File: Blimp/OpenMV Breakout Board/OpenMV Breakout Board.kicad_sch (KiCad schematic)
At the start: 20 parts, among them J1 UART3, J2 Detector, J3 Servo, J4 Debug, M1 OPENMV3, U1 ATWINC1500, U2 74LVC1G17

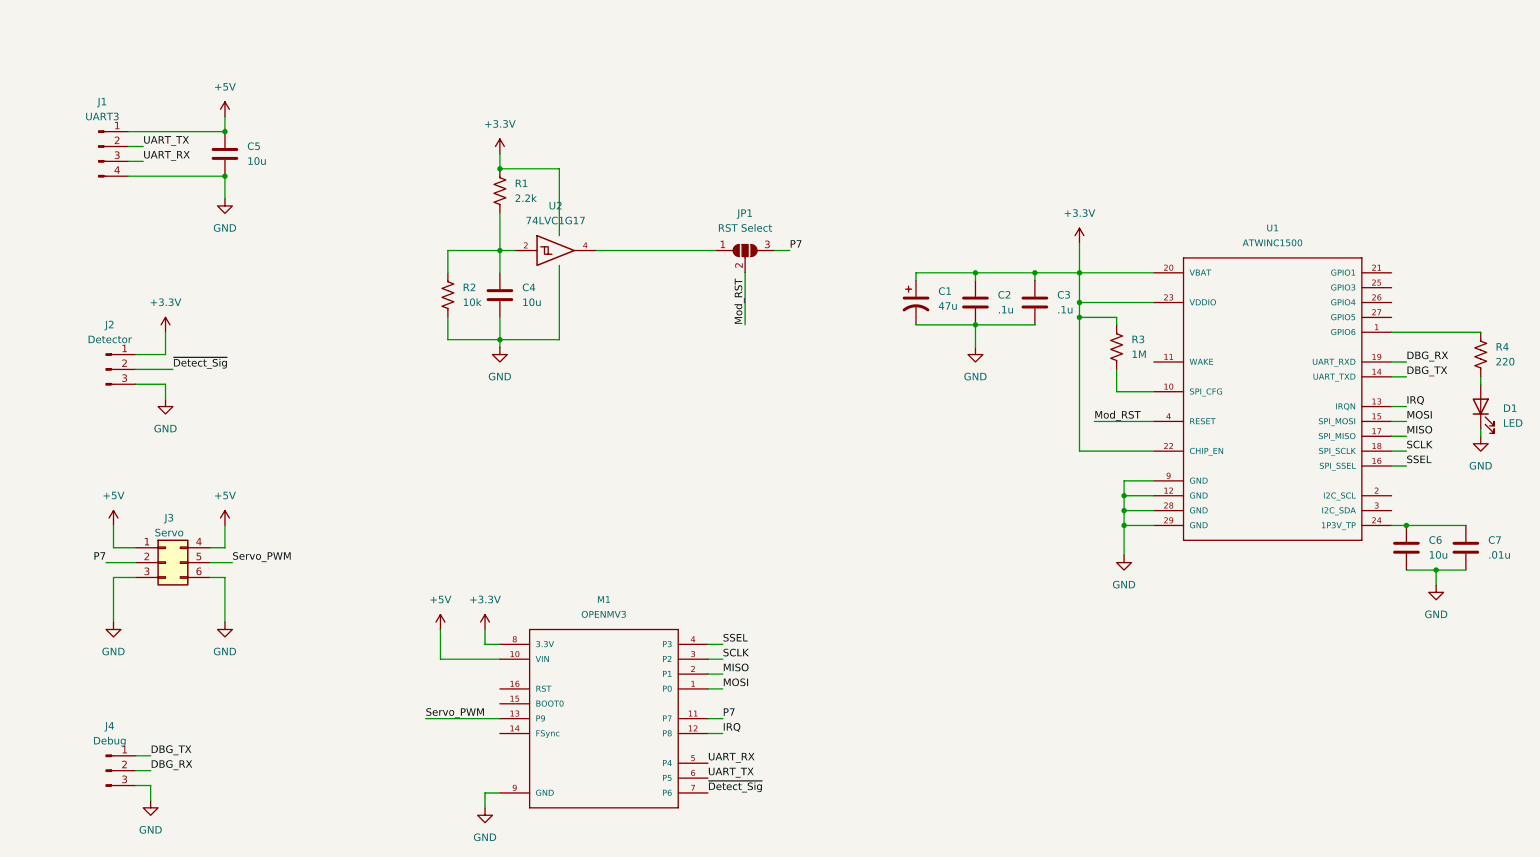
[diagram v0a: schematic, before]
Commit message: Updates to OpenMV hat to make pin labels more legible on PCB. Change schematic to be A paper sized for printing, reorg for readability
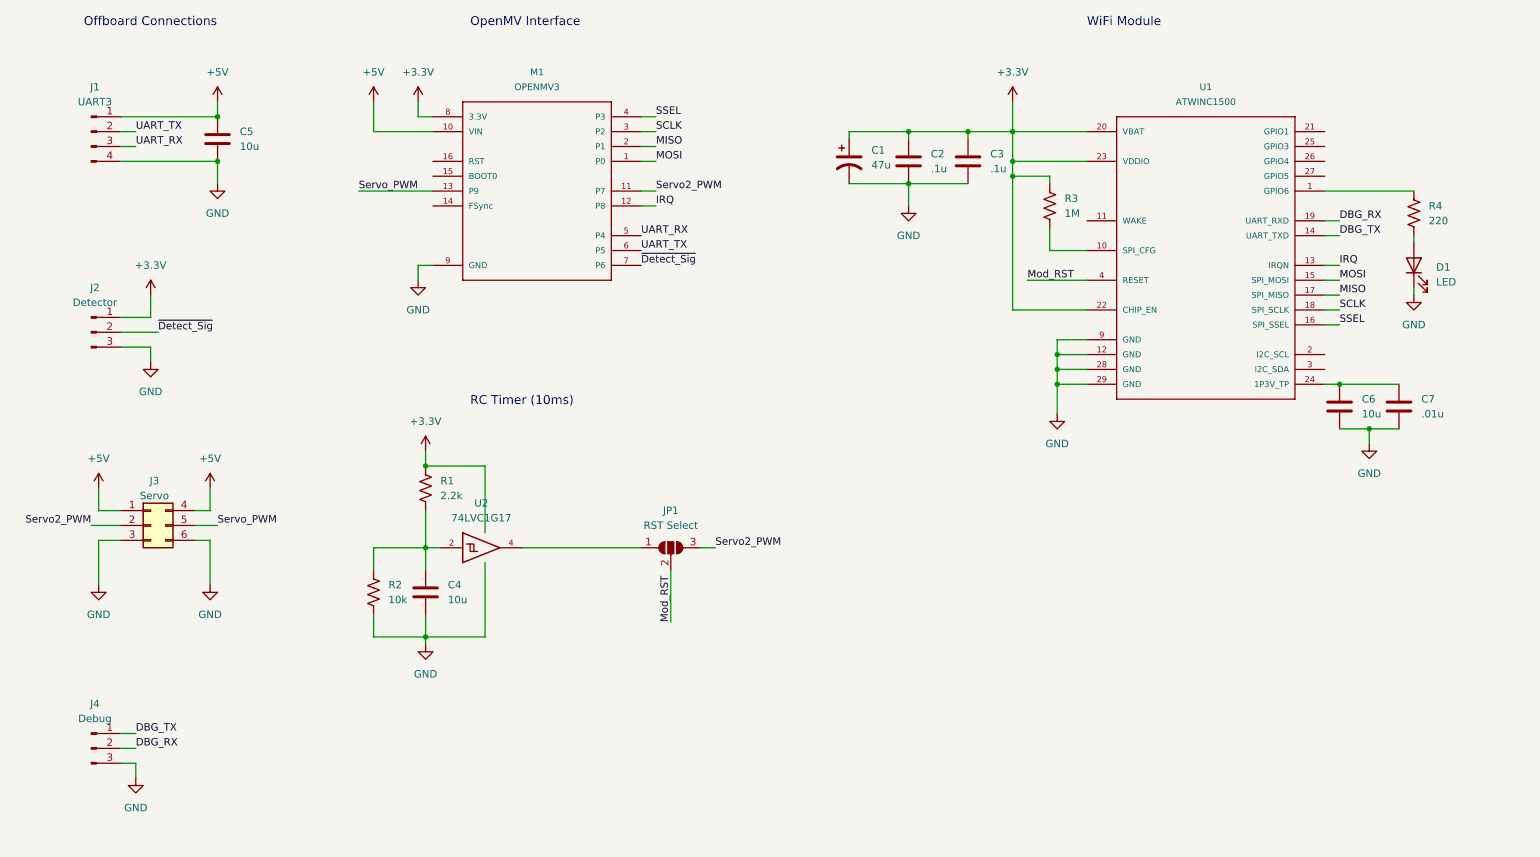
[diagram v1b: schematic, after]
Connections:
- net P7 renamed Servo2_PWM
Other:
- note added: "Offboard Connections"
- note added: "OpenMV Interface"
- note added: "RC Timer (10ms)"
- note added: "WiFi Module"
- moved on the sheet: C1, C2, C3, C4, C5, C6, C7, D1, J1, J2, J3, J4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
